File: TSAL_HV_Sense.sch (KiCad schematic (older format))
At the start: 16 parts, among them J1 2-1445098-2, J2 22035035, J3 2-1445098-2, J4 22035035, J5 22035065, U1 4N35, U2 4N35

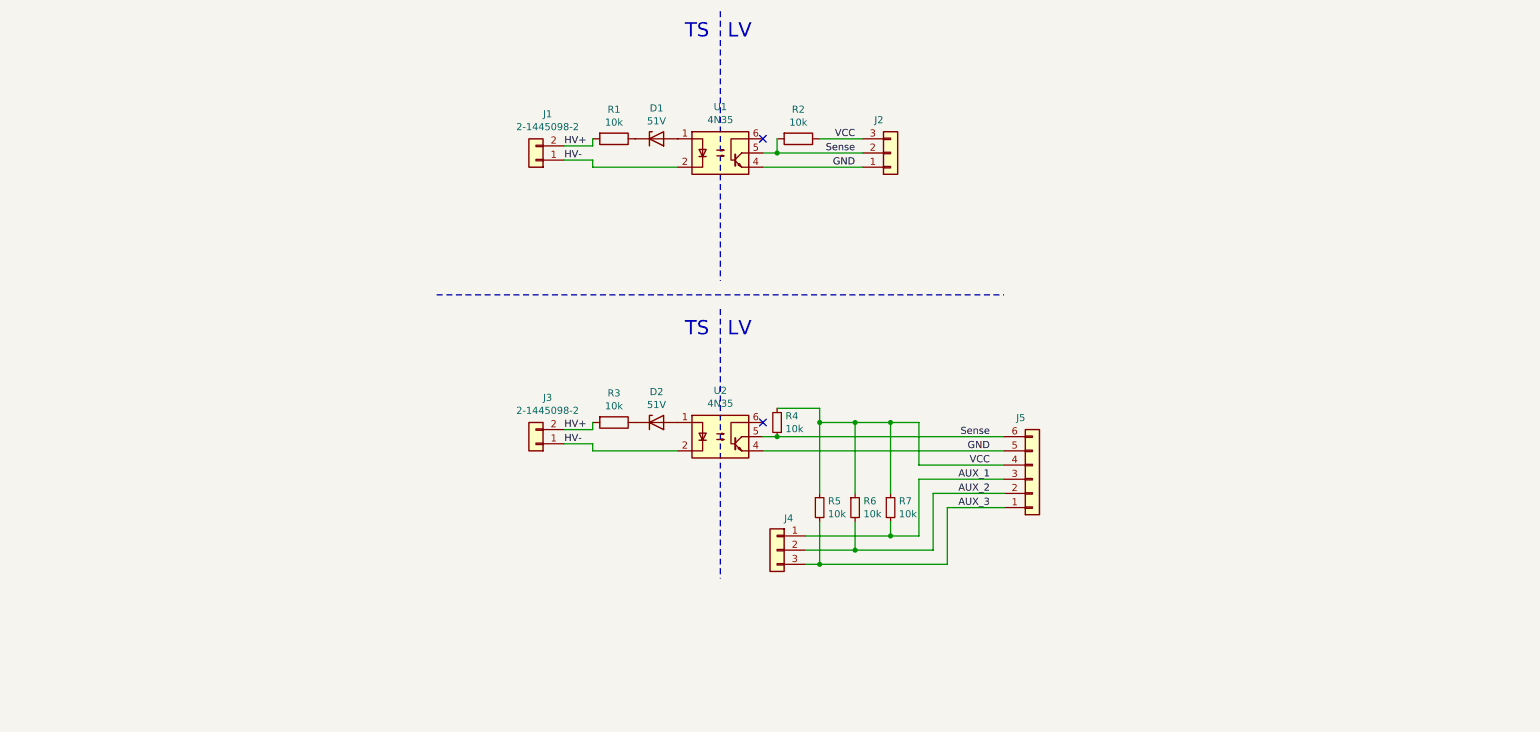
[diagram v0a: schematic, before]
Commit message: Redo HV sense boards
- added circuitry & connector for ts active led
- added led indicators for relay aux
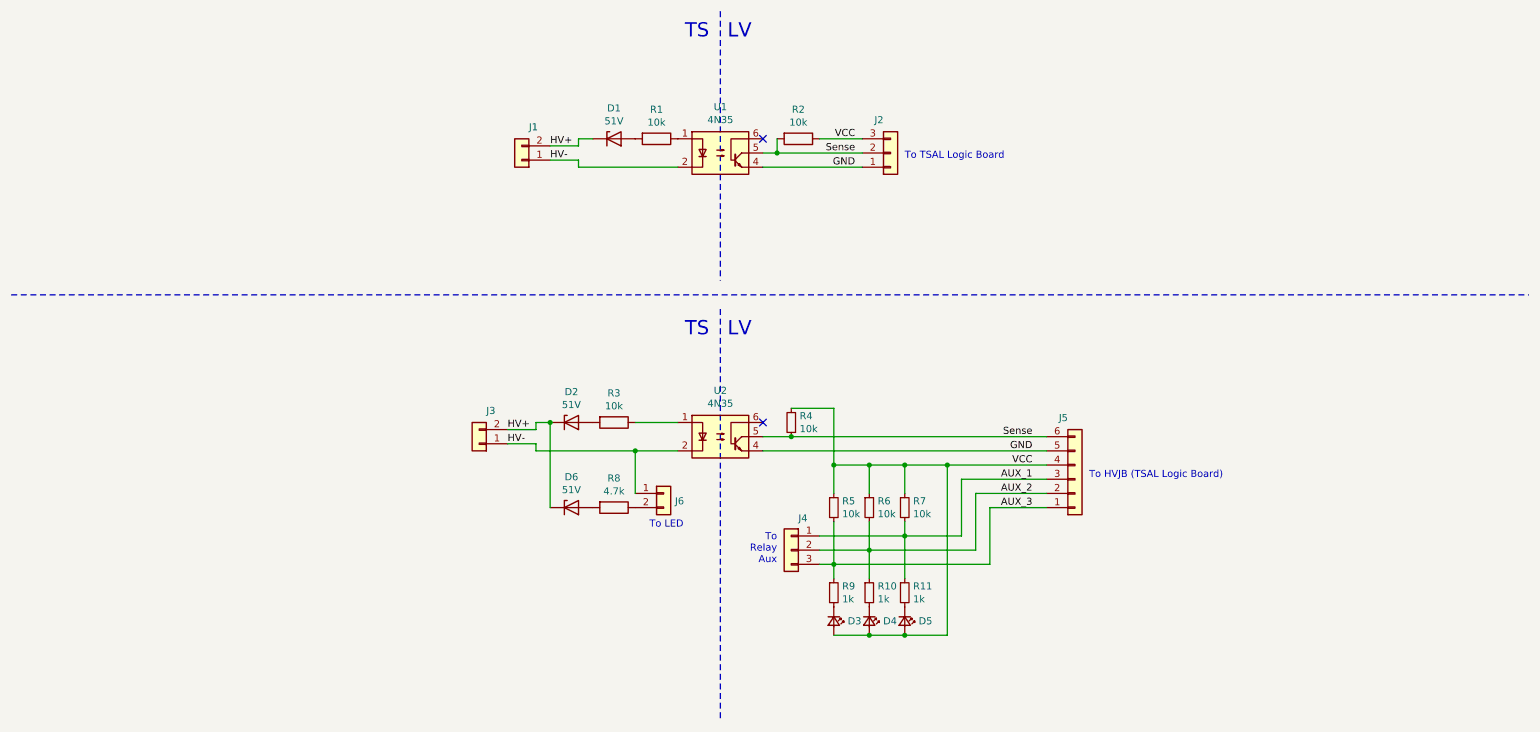
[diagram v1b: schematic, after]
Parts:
- added D3, D4, D5: LED, LED_THT:LED_D3.0mm, symbol Device:LED_Small
- added D6: 51V, Diode_THT:D_DO-41_SOD81_P10.16mm_Horizontal, symbol Device:D_Zener
- added J6: Conn_01x02, Connector_Molex:Molex_SPOX_5267-02A_1x02_P2.50mm_Vertical, symbol Connector_Generic:Conn_01x02
- added R10, R11, R9: 1k, Resistor_SMD:R_0805_2012Metric_Pad1.15x1.40mm_HandSolder, symbol Device:R_Small
- added R8: 4.7k, Resistor_THT:R_Axial_DIN0309_L9.0mm_D3.2mm_P12.70mm_Horizontal, symbol Device:R
- J1, J3: value 2-1445098-2 -> Nano-Fit; footprint project:TE_2-1445098-2 -> Connector_Molex:Molex_Nano-Fit_105309-xx02_1x02_P2.50mm_Vertical; Part (none) -> 105309-1102
- R2, R4, R5, R6, R7: footprint Resistor_THT:R_Axial_DIN0204_L3.6mm_D1.6mm_P5.08mm_Horizontal -> Resistor_SMD:R_0805_2012Metric_Pad1.15x1.40mm_HandSolder
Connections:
- net AUX_1: now also R11.1
- net AUX_2: now also R10.1
- net AUX_3: now also R9.1
- net HV+: now also D1.1 (K), D2.1 (K), D6.1 (K); no longer R1.2, R3.2
- net HV-: now also J6.1 (Pin_1)
- net VCC: now also D3.2 (A), D4.2 (A), D5.2 (A)
- net at U1.1: now also R1.1; no longer D1.2 (A)
- net at U2.1: now also R3.1; no longer D2.2 (A)
- new net: D1.2 (A), R1.2
- new net: D2.2 (A), R3.2
- new net: J6.2 (Pin_2), R8.1
- new net: D6.2 (A), R8.2
- new net: D3.1 (K), R9.2
- new net: D4.1 (K), R10.2
- new net: D5.1 (K), R11.2
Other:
- note added: "To HVJB (TSAL Logic Board)"
- note added: "To LED"
- note added: "To TSAL Logic Board"
- note added: "To\nRelay\nAux"
- moved on the sheet: D1, D2, J3, J4, J5, R1, R4, R5, R6, R7

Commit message: hv sense: include mechanical info in schematics
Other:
- note added: "HV Sense Board 1\nLocated in HV Junction Box"
- note added: "HV Sense Board 2\nLocated in Battery\nPower Electronics Compartment"
- note added: "Mechanical dimensions: 40mm x 40mm\nMounting holes: M3, 30mm x 30mm"
- note added: "Mechanical dimensions: 50mm x 50mm\nMounting holes: M3, 40mm x 40mm"
- note added: "To HV Indicator LED"
- note removed: "To LED"
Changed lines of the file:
@@
 Wire Wire Line
 	7100 4700 7800 4700
-Text Notes 5000 5150 0    50   ~ 0
-To LED
 $Comp
 L Device:D_Zener D2
@@
 	-1   0    0    1
 $EndComp
+Text Notes 1500 2000 0    60   ~ 0
+HV Sense Board 1\nLocated in HV Junction Box
+Text Notes 1500 4500 0    60   ~ 0
+HV Sense Board 2\nLocated in Battery\nPower Electronics Compartment
+Text Notes 1500 2500 0    60   ~ 0
+Mechanical dimensions: 40mm x 40mm\nMounting holes: M3, 30mm x 30mm
+Text Notes 1500 5000 0    60   ~ 0
+Mechanical dimensions: 50mm x 50mm\nMounting holes: M3, 40mm x 40mm
+Text Notes 5150 5200 2    50   ~ 0
+To HV Indicator LED
 $EndSCHEMATC

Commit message: tsal sense board update
hopefully last update
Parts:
- added R5: 2k, Resistor_THT:R_Axial_DIN0309_L9.0mm_D3.2mm_P12.70mm_Horizontal, symbol Device:R
- D3: renamed from D6; value 51V -> 30V; Part 1N5942B -> 1N5936B
- J2: value 22035035 -> Mini-SPOX; Part (none) -> 22035035
- J4: renamed from J6; value Conn_01x02 -> Mini-SPOX; Part (none) -> 22035025
- J5: renamed from J4; value 22035035 -> Mini-SPOX; Part (none) -> 22035035
- J6: renamed from J5; value 22035065 -> Mini-SPOX; Part (none) -> 22035065
- R1, R3: Part (none) -> RSMF1JT10K0
- R10: renamed from R9; Part (none) -> RC0805FR-071KL
- R11: renamed from R10; Part (none) -> RC0805FR-071KL
- R12: renamed from R11; Part (none) -> RC0805FR-071KL
- R2: Part (none) -> RC0805FR-0710KL
- R4: renamed from R8; value 4.7k -> 2k; Part (none) -> RSMF1JT2K00
- R6: renamed from R4; Part (none) -> RC0805FR-0710KL
- R7: renamed from R5; Part (none) -> RC0805FR-0710KL
- R8: renamed from R6; Part (none) -> RC0805FR-0710KL
- R9: renamed from R7; Part (none) -> RC0805FR-0710KL
- U1, U2: Part (none) -> 4N35
- renumbered D3 to D4, D4 to D5, D5 to D6
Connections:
- net at R4.1: now also R5.2; no longer J4.2 (Pin_2)
- new net: J4.2 (Pin_2), R5.1
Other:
- note added: "To HV\nIndicator LED"
- note removed: "To HV Indicator LED"
- moved on the sheet: D2, D3, J3, R3, R4

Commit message: oops obsolete part
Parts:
- D3: value 30V -> 33V; Part 1N5936B -> 1N5937B
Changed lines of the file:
@@
 P 4150 5000
 F 0 "D3" H 4150 5216 50  0000 C CNN
-F 1 "30V" H 4150 5125 50  0000 C CNN
+F 1 "33V" H 4150 5125 50  0000 C CNN
 F 2 "Diode_THT:D_DO-41_SOD81_P10.16mm_Horizontal" H 4150 5000 50  0001 C CNN
 F 3 "~" H 4150 5000 50  0001 C CNN
-F 4 "1N5936B" H 4150 5000 50  0001 C CNN "Part"
+F 4 "1N5937B" H 4150 5000 50  0001 C CNN "Part"
 	1    4150 5000
 	1    0    0    -1
